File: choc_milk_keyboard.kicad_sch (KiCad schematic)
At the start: 6 parts, among them J1 Conn_01x02_Female, SW1 SW_PUSH, SW2 SW_PUSH, U1 ProMicro

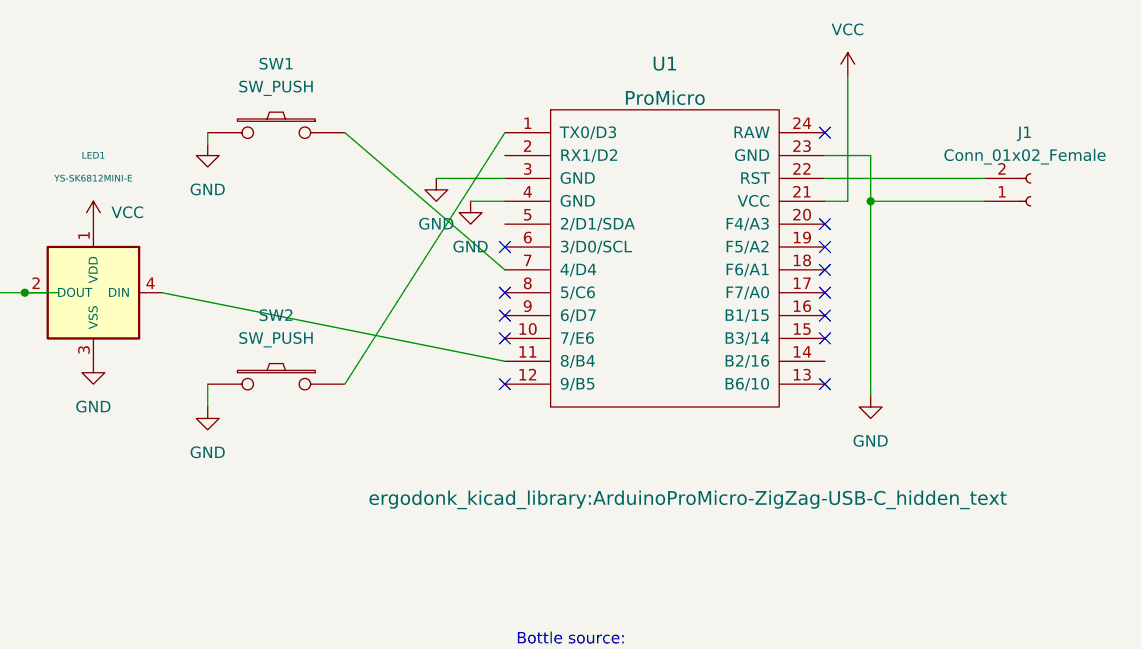
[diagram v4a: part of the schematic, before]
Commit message: Logo rework, rewire to use classic firmware, silkscreeen tidy
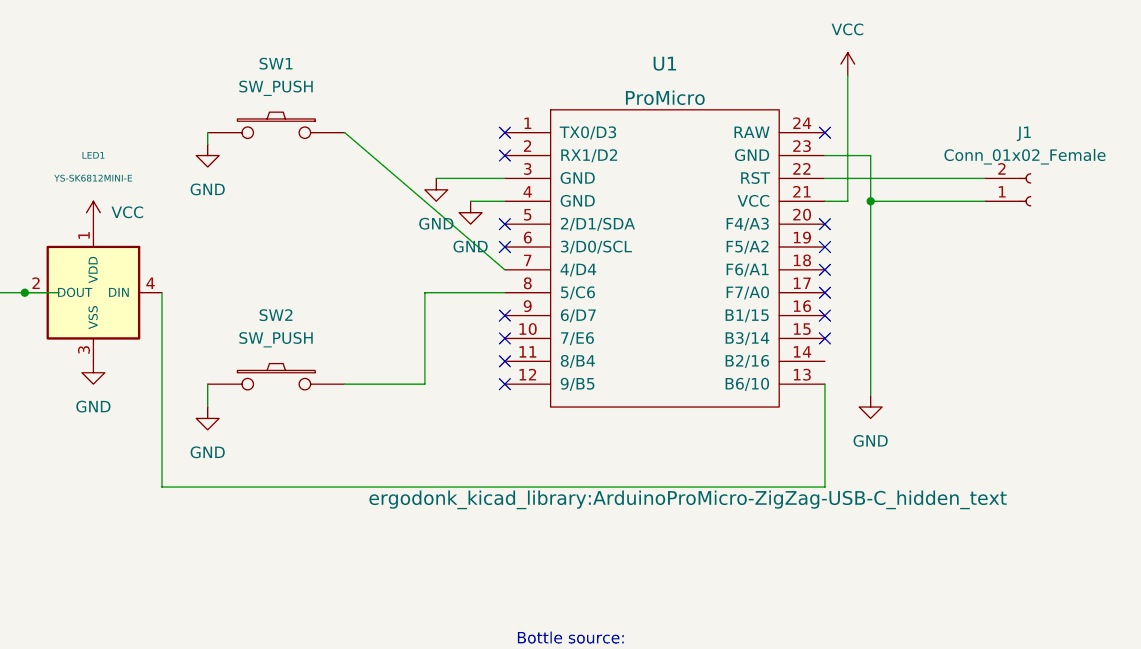
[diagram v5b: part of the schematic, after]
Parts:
- SW1, SW2: footprint ergodonk_kicad_library:Low-Profile-Choc-MX_no_text -> ergodonk_kicad_library:Low-Profile-Choc-MX_no_text_V2
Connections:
- net at U1.1 (TX0/D3): no longer SW2.1
- net at U1.11 (8/B4): no longer LED1.4 (DIN)
- net at U1.13 (B6/10): now also LED1.4 (DIN)
- net at U1.8 (5/C6): now also SW2.1
- no-connect marks 13 -> 15

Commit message: Moved footprints to new library Sent this version out for production Added tweezer holes to LEDs Cleaned up microcontroller footprint
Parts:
- LED1, LED2: footprint Keebio-Parts:SK6812-MINI-E -> Choc-milk-parts:SK6812-MINI-E
- SW1, SW2: footprint ergodonk_kicad_library:Low-Profile-Choc-MX_no_text_V2 -> Choc-milk-parts:Low-Profile-MX-Choc-V1-V2
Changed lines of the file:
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@@
       (effects (font (size 1.27 1.27)))
     )
-    (property "Footprint" "ergodonk_kicad_library:Low-Profile-Choc-MX_no_text_V2" (at 118.11 101.6 0)
+    (property "Footprint" "Choc-milk-parts:Low-Profile-MX-Choc-V1-V2" (at 118.11 101.6 0)
       (effects (font (size 1.27 1.27)) hide)
     )
@@
       (effects (font (size 0.7366 0.7366)))
     )
-    (property "Footprint" "Keebio-Parts:SK6812-MINI-E" (at 76.2 97.79 0)
+    (property "Footprint" "Choc-milk-parts:SK6812-MINI-E" (at 76.2 97.79 0)
       (effects (font (size 1.27 1.27)) hide)
     )
@@
       (effects (font (size 0.7366 0.7366)))
     )
-    (property "Footprint" "Keebio-Parts:SK6812-MINI-E" (at 95.25 97.79 0)
+    (property "Footprint" "Choc-milk-parts:SK6812-MINI-E" (at 95.25 97.79 0)
       (effects (font (size 1.27 1.27)) hide)
     )
@@
       (effects (font (size 1.27 1.27)))
     )
-    (property "Footprint" "ergodonk_kicad_library:Low-Profile-Choc-MX_no_text_V2" (at 118.11 73.66 0)
+    (property "Footprint" "Choc-milk-parts:Low-Profile-MX-Choc-V1-V2" (at 118.11 73.66 0)
       (effects (font (size 1.27 1.27)) hide)
     )
